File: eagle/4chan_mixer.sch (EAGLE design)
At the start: 29 parts, among them IC1 TL072P

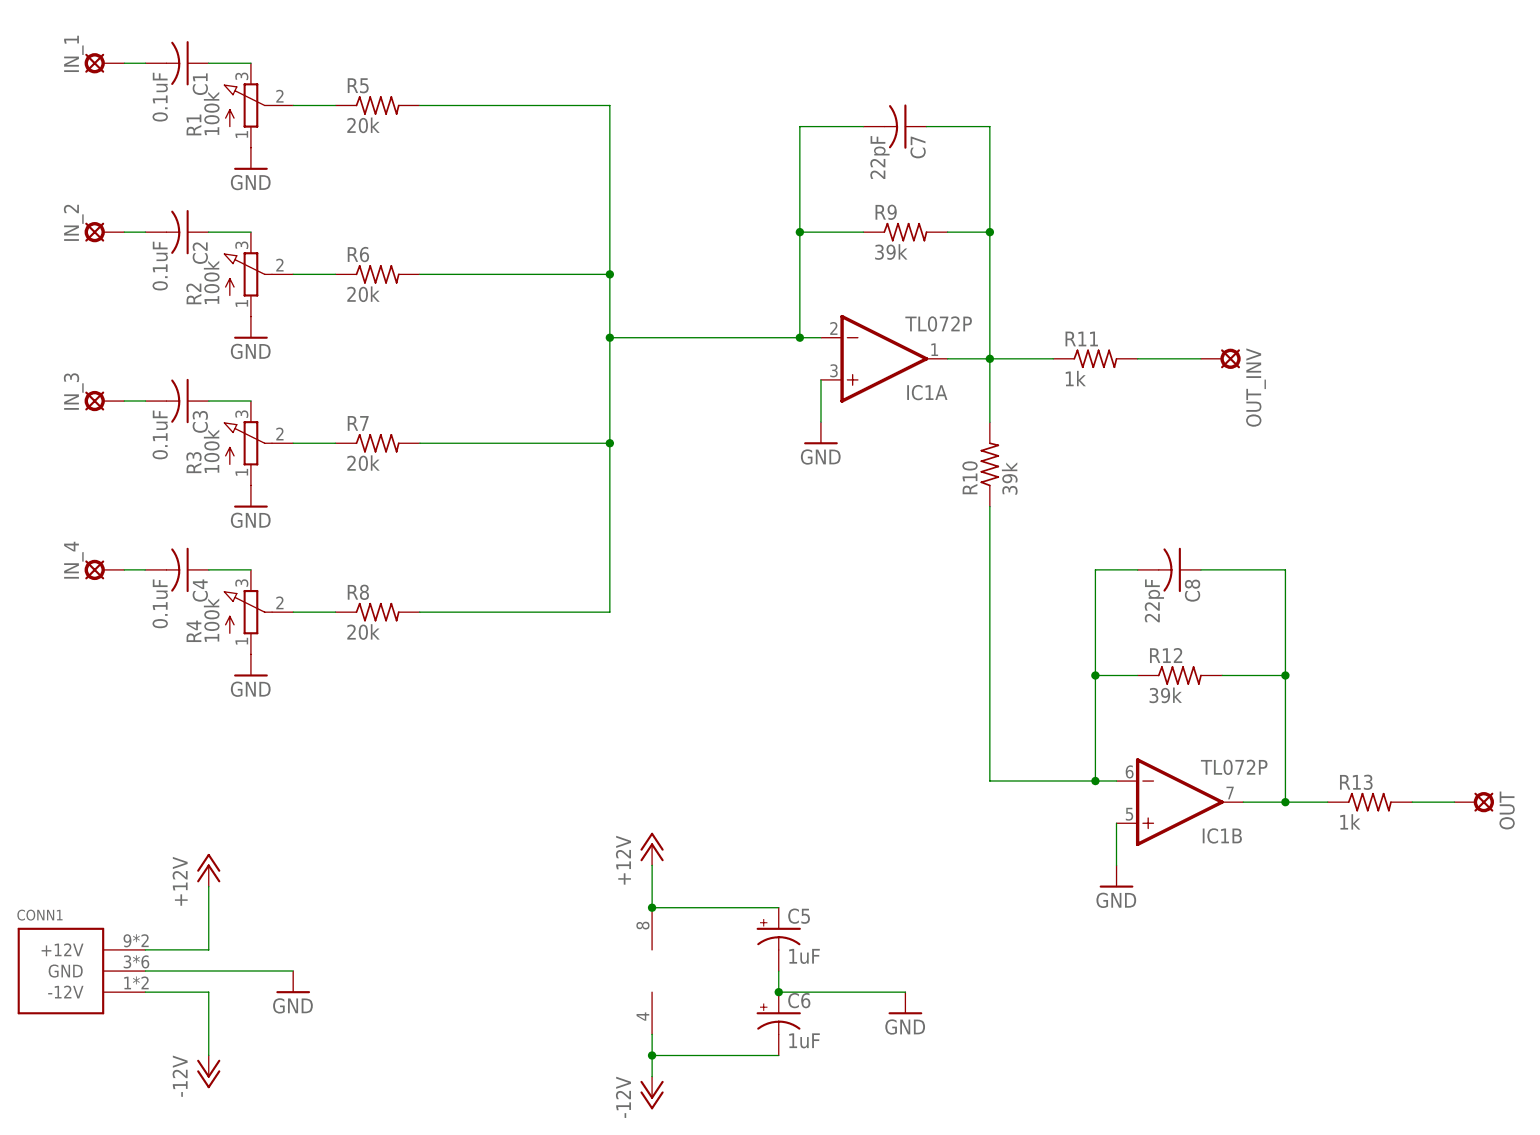
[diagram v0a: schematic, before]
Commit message: grounds and cutout path for cnc
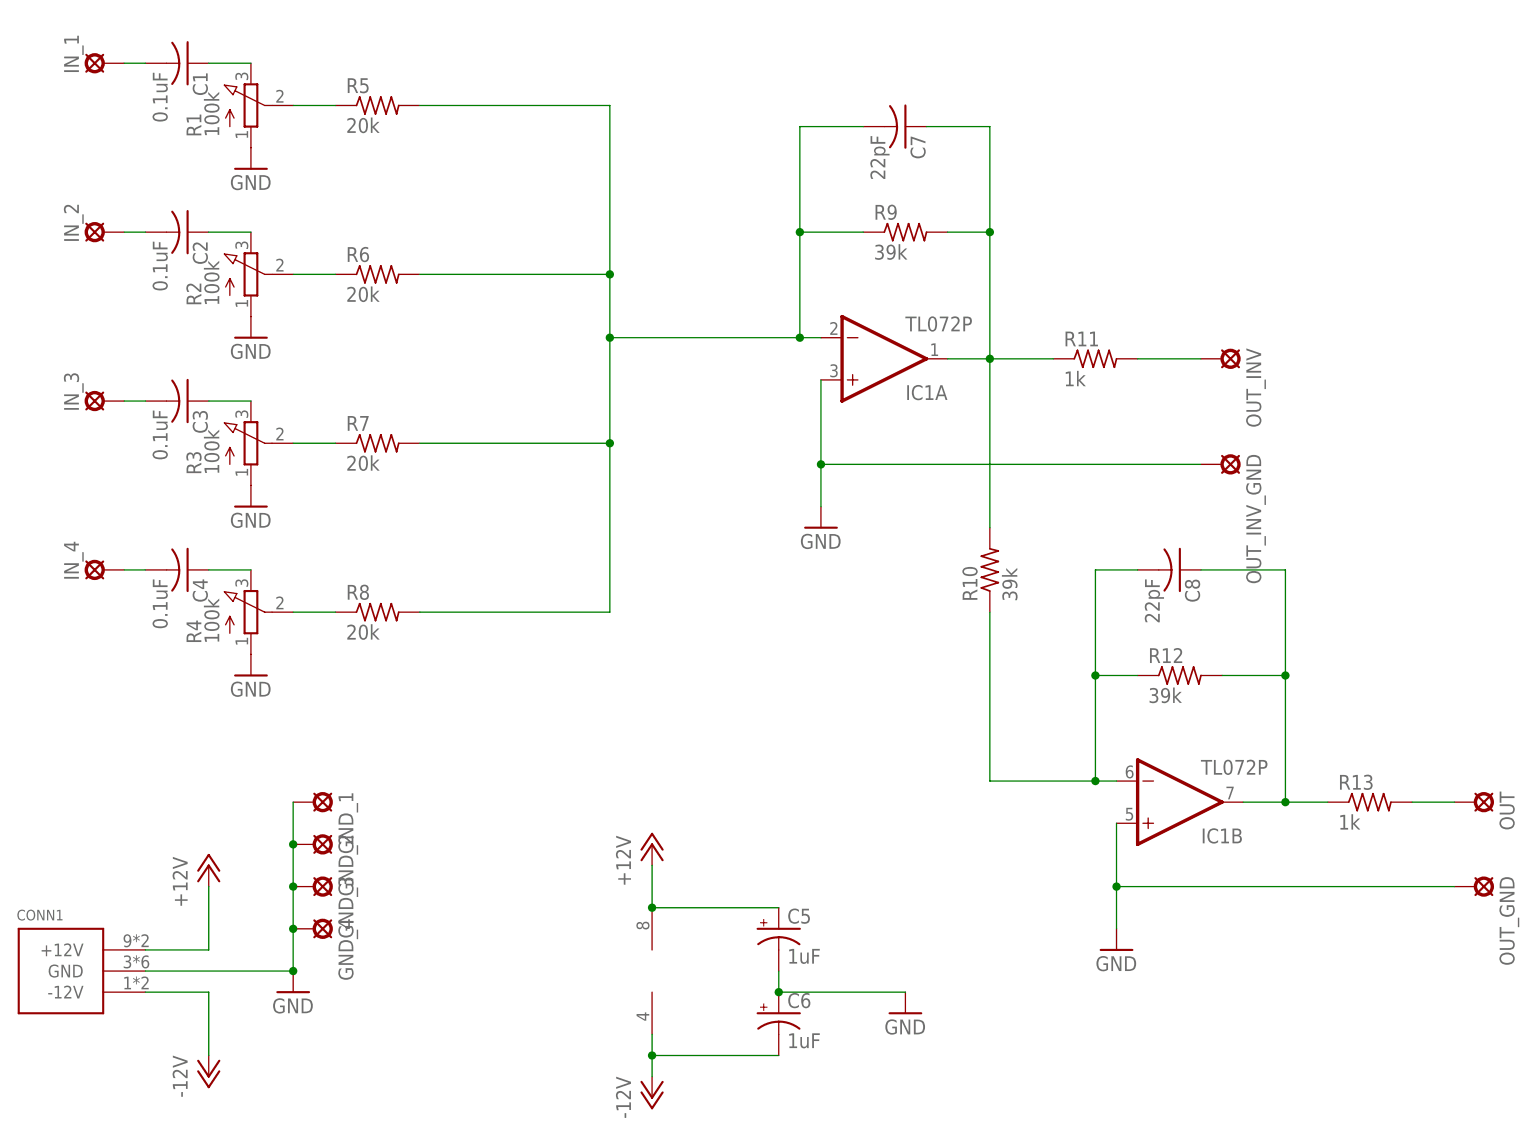
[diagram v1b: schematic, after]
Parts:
- added GND_1, GND_2, GND_3, GND_4, OUT_GND, OUT_INV_GND: LSP11, solpad:LSP11
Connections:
- net GND: now also GND_1.MP, GND_2.MP, GND_3.MP, GND_4.MP, OUT_GND.MP, OUT_INV_GND.MP
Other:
- moved on the sheet: R10
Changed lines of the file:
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@@
 <part name="R12" library="rcl" deviceset="R-US_" device="0207/7" value="39k"/>
 <part name="C8" library="rcl" deviceset="C-US" device="050-030X075" value="22pF"/>
+<part name="GND_1" library="solpad" deviceset="LSP11" device=""/>
+<part name="GND_2" library="solpad" deviceset="LSP11" device=""/>
+<part name="GND_3" library="solpad" deviceset="LSP11" device=""/>
+<part name="GND_4" library="solpad" deviceset="LSP11" device=""/>
+<part name="OUT_GND" library="solpad" deviceset="LSP11" device=""/>
+<part name="OUT_INV_GND" library="solpad" deviceset="LSP11" device=""/>
 </parts>
 <sheets>
@@
 <instance part="C6" gate="G$1" x="78.74" y="2.54"/>
 <instance part="GND7" gate="1" x="93.98" y="2.54"/>
-<instance part="GND6" gate="1" x="83.82" y="71.12"/>
-<instance part="GND8" gate="1" x="119.38" y="17.78"/>
+<instance part="GND6" gate="1" x="83.82" y="60.96"/>
+<instance part="GND8" gate="1" x="119.38" y="10.16"/>
 <instance part="IN_3" gate="1" x="-2.54" y="76.2" rot="R90"/>
 <instance part="C3" gate="G$1" x="7.62" y="76.2" rot="R270"/>
@@
 <instance part="GND1" gate="1" x="15.24" y="104.14"/>
 <instance part="R13" gate="G$1" x="149.86" y="27.94"/>
-<instance part="R10" gate="G$1" x="104.14" y="68.58" rot="R90"/>
+<instance part="R10" gate="G$1" x="104.14" y="55.88" rot="R90"/>
 <instance part="R12" gate="G$1" x="127" y="43.18"/>
 <instance part="C8" gate="G$1" x="127" y="55.88" rot="R270"/>
+<instance part="GND_1" gate="1" x="22.86" y="27.94" rot="R270"/>
+<instance part="GND_2" gate="1" x="22.86" y="22.86" rot="R270"/>
+<instance part="GND_3" gate="1" x="22.86" y="17.78" rot="R270"/>
+<instance part="GND_4" gate="1" x="22.86" y="12.7" rot="R270"/>
+<instance part="OUT_GND" gate="1" x="162.56" y="17.78" rot="R270"/>
+<instance part="OUT_INV_GND" gate="1" x="132.08" y="68.58" rot="R270"/>
 </instances>
 <busses>
@@
 <pinref part="GND5" gate="1" pin="GND"/>
 <wire x1="2.54" y1="7.62" x2="20.32" y2="7.62" width="0.1524" layer="91"/>
+<pinref part="GND_1" gate="1" pin="MP"/>
+<pinref part="GND_2" gate="1" pin="MP"/>
+<wire x1="20.32" y1="27.94" x2="20.32" y2="22.86" width="0.1524" layer="91"/>
+<pinref part="GND_3" gate="1" pin="MP"/>
+<wire x1="20.32" y1="22.86" x2="20.32" y2="17.78" width="0.1524" layer="91"/>
+<junction x="20.32" y="22.86"/>
+<pinref part="GND_4" gate="1" pin="MP"/>
+<wire x1="20.32" y1="17.78" x2="20.32" y2="12.7" width="0.1524" layer="91"/>
+<junction x="20.32" y="17.78"/>
+<wire x1="20.32" y1="12.7" x2="20.32" y2="7.62" width="0.1524" layer="91"/>
+<junction x="20.32" y="12.7"/>
+<junction x="20.32" y="7.62"/>
 </segment>
 <segment>
@@
 <pinref part="IC1" gate="A" pin="+IN"/>
 <pinref part="GND6" gate="1" pin="GND"/>
-<wire x1="83.82" y1="73.66" x2="83.82" y2="78.74" width="0.1524" layer="91"/>
+<wire x1="83.82" y1="63.5" x2="83.82" y2="68.58" width="0.1524" layer="91"/>
+<pinref part="OUT_INV_GND" gate="1" pin="MP"/>
+<wire x1="83.82" y1="68.58" x2="83.82" y2="78.74" width="0.1524" layer="91"/>
+<wire x1="129.54" y1="68.58" x2="83.82" y2="68.58" width="0.1524" layer="91"/>
+<junction x="83.82" y="68.58"/>
 </segment>
 <segment>
 <pinref part="IC1" gate="B" pin="+IN"/>
 <pinref part="GND8" gate="1" pin="GND"/>
-<wire x1="119.38" y1="20.32" x2="119.38" y2="25.4" width="0.1524" layer="91"/>
+<wire x1="119.38" y1="12.7" x2="119.38" y2="17.78" width="0.1524" layer="91"/>
+<pinref part="OUT_GND" gate="1" pin="MP"/>
+<wire x1="119.38" y1="17.78" x2="119.38" y2="25.4" width="0.1524" layer="91"/>
+<wire x1="160.02" y1="17.78" x2="119.38" y2="17.78" width="0.1524" layer="91"/>
+<junction x="119.38" y="17.78"/>
 </segment>
 <segment>
@@
 <junction x="104.14" y="96.52"/>
 <pinref part="R10" gate="G$1" pin="2"/>
-<wire x1="104.14" y1="73.66" x2="104.14" y2="81.28" width="0.1524" layer="91"/>
+<wire x1="104.14" y1="60.96" x2="104.14" y2="81.28" width="0.1524" layer="91"/>
 </segment>
 </net>
@@
 <wire x1="119.38" y1="30.48" x2="116.84" y2="30.48" width="0.1524" layer="91"/>
 <pinref part="R10" gate="G$1" pin="1"/>
-<wire x1="104.14" y1="63.5" x2="104.14" y2="30.48" width="0.1524" layer="91"/>
+<wire x1="104.14" y1="50.8" x2="104.14" y2="30.48" width="0.1524" layer="91"/>
 <wire x1="104.14" y1="30.48" x2="116.84" y2="30.48" width="0.1524" layer="91"/>
 <junction x="116.84" y="30.48"/>

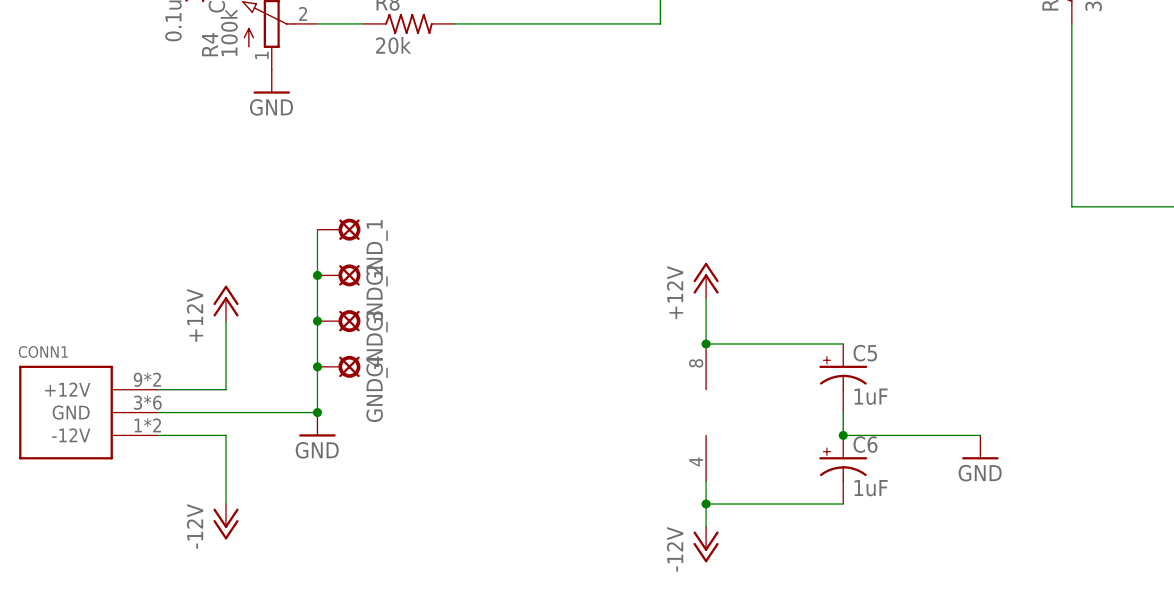
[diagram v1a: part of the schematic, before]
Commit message: now with ferrite bead filters and decouple caps closer to opamp
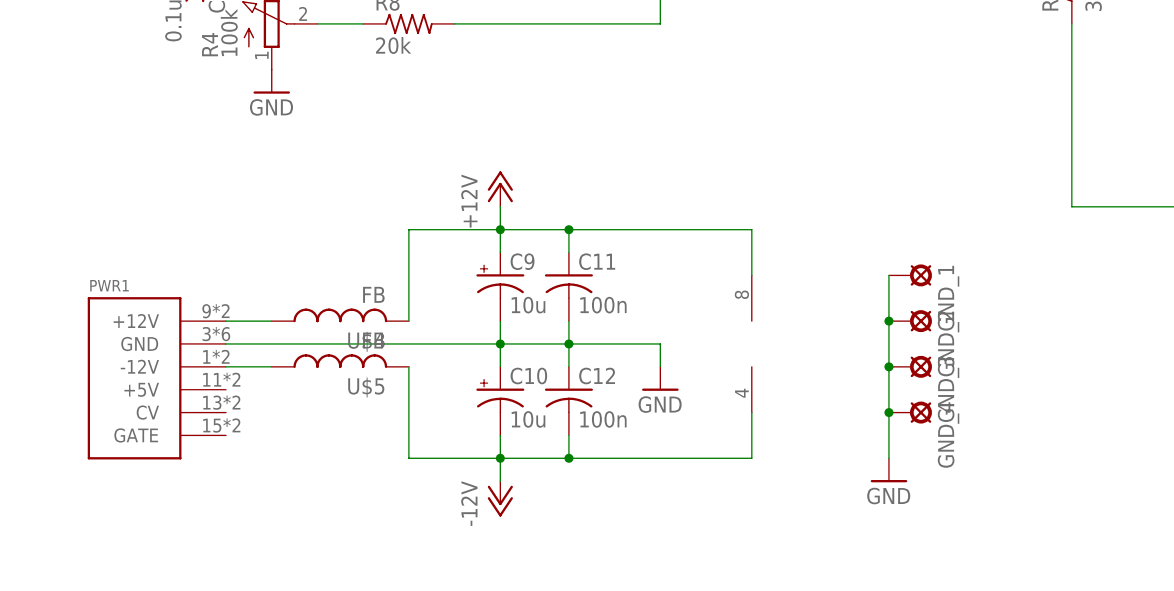
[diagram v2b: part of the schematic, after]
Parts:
- removed C5, C6: 1uF, rcl:CPOL-USB45181A
- removed CONN1: POWER_SIMPLE10, eurorack:POWER_SIMPLE10
- added C10, C9: 10u, rcl:CPOL-USB45181A
- added C11, C12: 100n, rcl:C-US050-024X044
- added PWR1: POWER, eurorack:POWER
- added U$4, U$5: FB, adafruit:FB
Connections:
- new net N$20: PWR1.-12V, U$5.1
- new net N$6: PWR1.+12V, U$4.1
- net +12V: now also C11.1, C9.+, U$4.2; no longer C5.+, CONN1.+12V
- net -12V: now also C10.-, C12.2, U$5.2; no longer C6.-, CONN1.-12V
- net GND: now also C10.+, C11.2, C12.1, C9.-, PWR1.GND; no longer C5.-, C6.+, CONN1.GND
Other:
- moved on the sheet: GND_1, GND_2, GND_3, GND_4
